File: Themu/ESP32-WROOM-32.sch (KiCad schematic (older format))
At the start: 17 parts, among them J1 USB_B_Micro, Q1 mmbt2222, Q2 mmbt2222, U1 CP2104, U3 ESP32-WROOM-32

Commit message: Routed completed
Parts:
- removed D1: RED LED, LED_SMD:LED_0603_1608Metric_Pad1.05x0.95mm_HandSolder, symbol Device:LED_Small_ALT
- added L1: RGB LED, LED APTF1616LSEEZGKQBKC:LED APTF1616LSEEZGKQBKC, symbol LED:ASMB-MTB1-0A3A2
- added R20, R21: 1K, Resistor_SMD:R_0603_1608Metric_Pad1.05x0.95mm_HandSolder, symbol Device:R_Small_US
- U3: footprint RF_Module:ESP32-WROOM-32 -> Themu_FP_Lib:ESP32WROOM32D
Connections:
- net +3V3: now also L1.4 (A); no longer R3.1
- net BTN: now also U3.10 (IO25); no longer U3.14 (IO12)
- net FLX2: now also U3.6 (IO34); no longer U3.8 (IO32)
- net FLX3: now also U3.7 (IO35); no longer U3.9 (IO33)
- net FLX4: now also U3.8 (IO32); no longer U3.6 (IO34)
- net FLX5: now also U3.9 (IO33); no longer U3.7 (IO35)
- net IO26: now reaches U3.11 (IO26)
- net IO26: now also R20.1
- net IO27: now reaches U3.12 (IO27)
- net IO27: now also R21.1
- net at R3.2: now also L1.3 (BK)
- net IO13: no longer names the net of U3.16 (IO13)
- new net: L1.1 (RK), R21.2
- new net: L1.2 (GK), R20.2
- new net IO12: R3.1, U3.14 (IO12)
- no-connect marks 33 -> 31
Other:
- moved on the sheet: R4, R5
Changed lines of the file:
@@
 	1    0    0    -1
 $EndComp
-NoConn ~ 3400 3650
-NoConn ~ 3400 3550
-NoConn ~ 3400 3450
 NoConn ~ 3400 3350
 NoConn ~ 3400 3250
@@
 ADC1_CH7
 Wire Wire Line
-	1050 3800 1500 3800
-Wire Wire Line
-	1050 3700 1050 3800
+	1100 2550 1550 2550
+Wire Wire Line
+	1100 2450 1100 2550
 $Comp
 L power:GND #PWR?
 U 1 1 5F674CFE
-P 1050 4100
+P 1100 2850
 AR Path="/5F674CFE" Ref="#PWR?"  Part="1"
 AR Path="/5F4501E0/5F674CFE" Ref="#PWR07"  Part="1"
-F 0 "#PWR07" H 1050 3850 50  0001 C CNN
-F 1 "GND" H 1055 3927 50  0000 C CNN
-F 2 "" H 1050 4100 50  0001 C CNN
-F 3 "" H 1050 4100 50  0001 C CNN
-	1    1050 4100
+F 0 "#PWR07" H 1100 2600 50  0001 C CNN
+F 1 "GND" H 1105 2677 50  0000 C CNN
+F 2 "" H 1100 2850 50  0001 C CNN
+F 3 "" H 1100 2850 50  0001 C CNN
+	1    1100 2850
 	1    0    0    -1
 $EndComp
@@
 L Device:R_Small_US R?
 U 1 1 5F674D0A
-P 1050 3600
+P 1100 2350
 AR Path="/5F674D0A" Ref="R?"  Part="1"
 AR Path="/5F4501E0/5F674D0A" Ref="R4"  Part="1"
-F 0 "R4" H 1118 3646 50  0000 L CNN
-F 1 "100K" H 1118 3555 50  0000 L CNN
-F 2 "Resistor_SMD:R_0603_1608Metric_Pad1.05x0.95mm_HandSolder" H 1050 3600 50  0001 C CNN
-F 3 "https://www.bourns.com/docs/product-datasheets/CRxxxxx.pdf" H 1050 3600 50  0001 C CNN
-F 4 "CR0603-FX-1003ELF" H 1050 3600 50  0001 C CNN "*Digikey"
-	1    1050 3600
+F 0 "R4" H 1168 2396 50  0000 L CNN
+F 1 "100K" H 1168 2305 50  0000 L CNN
+F 2 "Resistor_SMD:R_0603_1608Metric_Pad1.05x0.95mm_HandSolder" H 1100 2350 50  0001 C CNN
+F 3 "https://www.bourns.com/docs/product-datasheets/CRxxxxx.pdf" H 1100 2350 50  0001 C CNN
+F 4 "CR0603-FX-1003ELF" H 1100 2350 50  0001 C CNN "*Digikey"
+	1    1100 2350
 	1    0    0    -1
 $EndComp
@@
 L Device:R_Small_US R?
 U 1 1 5F677550
-P 1050 3950
+P 1100 2700
 AR Path="/5F677550" Ref="R?"  Part="1"
 AR Path="/5F4501E0/5F677550" Ref="R5"  Part="1"
-F 0 "R5" H 1118 3996 50  0000 L CNN
-F 1 "100K" H 1118 3905 50  0000 L CNN
-F 2 "Resistor_SMD:R_0603_1608Metric_Pad1.05x0.95mm_HandSolder" H 1050 3950 50  0001 C CNN
-F 3 "https://www.bourns.com/docs/product-datasheets/CRxxxxx.pdf" H 1050 3950 50  0001 C CNN
-F 4 "CR0603-FX-1003ELF" H 1050 3950 50  0001 C CNN "*Digikey"
-	1    1050 3950
-	1    0    0    -1
-$EndComp
-Wire Wire Line
-	1050 3800 1050 3850
-Wire Wire Line
-	1050 4050 1050 4100
-Connection ~ 1050 3800
+F 0 "R5" H 1168 2746 50  0000 L CNN
+F 1 "100K" H 1168 2655 50  0000 L CNN
+F 2 "Resistor_SMD:R_0603_1608Metric_Pad1.05x0.95mm_HandSolder" H 1100 2700 50  0001 C CNN
+F 3 "https://www.bourns.com/docs/product-datasheets/CRxxxxx.pdf" H 1100 2700 50  0001 C CNN
+F 4 "CR0603-FX-1003ELF" H 1100 2700 50  0001 C CNN "*Digikey"
+	1    1100 2700
+	1    0    0    -1
+$EndComp
+Wire Wire Line
+	1100 2550 1100 2600
+Wire Wire Line
+	1100 2800 1100 2850
+Connection ~ 1100 2550
 $Comp
 L power:+BATT #PWR06
 U 1 1 5F67B0FC
-P 1050 3500
-F 0 "#PWR06" H 1050 3350 50  0001 C CNN
-F 1 "+BATT" H 1065 3673 50  0000 C CNN
-F 2 "" H 1050 3500 50  0001 C CNN
-F 3 "" H 1050 3500 50  0001 C CNN
-	1    1050 3500
+P 1100 2250
+F 0 "#PWR06" H 1100 2100 50  0001 C CNN
+F 1 "+BATT" H 1115 2423 50  0000 C CNN
+F 2 "" H 1100 2250 50  0001 C CNN
+F 3 "" H 1100 2250 50  0001 C CNN
+	1    1100 2250
 	1    0    0    -1
 $EndComp
@@
 Wire Wire Line
 	2200 1750 2100 1750
-$Comp
-L Device:LED_Small_ALT D?
-U 1 1 5F6888D7
-P 1050 2850
-AR Path="/5F6888D7" Ref="D?"  Part="1"
-AR Path="/5F4501E0/5F6888D7" Ref="D1"  Part="1"
-F 0 "D1" V 1096 2780 50  0000 R CNN
-F 1 "RED LED" V 1005 2780 50  0000 R CNN
-F 2 "LED_SMD:LED_0603_1608Metric_Pad1.05x0.95mm_HandSolder" V 1050 2850 50  0001 C CNN
-F 3 "https://www.aopled.com/AOP_PDFs/L196L-UEC.pdf" V 1050 2850 50  0001 C CNN
-F 4 "L196L-UEC" H 1050 2850 50  0001 C CNN "*Digikey"
-	1    1050 2850
-	0    -1   -1   0
-$EndComp
 $Comp
 L power:VBUS #PWR01
@@
 Wire Wire Line
 	5100 2600 5300 2600
-Text Label 1300 3050 2    50   ~ 0
-IO13
-$Comp
-L Device:R_Small_US R3
-U 1 1 5F7258DA
-P 1050 2600
-F 0 "R3" H 1118 2646 50  0000 L CNN
-F 1 "1K" H 1118 2555 50  0000 L CNN
-F 2 "Resistor_SMD:R_0603_1608Metric_Pad1.05x0.95mm_HandSolder" H 1050 2600 50  0001 C CNN
-F 3 "https://www.bourns.com/docs/product-datasheets/CRxxxxx.pdf" H 1050 2600 50  0001 C CNN
-F 4 "CR0603-FX-1001ELF" H 1050 2600 50  0001 C CNN "*Digikey"
-	1    1050 2600
-	1    0    0    -1
-$EndComp
-Wire Wire Line
-	1050 2750 1050 2700
-Wire Wire Line
-	1050 2500 1050 2450
-Wire Wire Line
-	1050 3050 1300 3050
 NoConn ~ 6100 2400
 NoConn ~ 6100 2500
@@
 NoConn ~ 7500 1700
 NoConn ~ 7500 1600
-Text Label 3650 2450 2    50   ~ 0
-IO13
-Wire Wire Line
-	3400 2450 3650 2450
 Wire Notes Line
 	4350 850  7850 850
@@
 F 0 "U3" H 2800 4531 50  0000 C CNN
 F 1 "ESP32-WROOM-32" H 2800 4440 50  0000 C CNN
-F 2 "RF_Module:ESP32-WROOM-32" H 2800 1450 50  0001 C CNN
+F 2 "Themu_FP_Lib:ESP32WROOM32D" H 2800 1450 50  0001 C CNN
 F 3 "https://www.espressif.com/sites/default/files/documentation/esp32-wroom-32_datasheet_en.pdf" H 2500 3000 50  0001 C CNN
 F 4 "1965-ESP32-WROOM-32D(4MB)CT-ND" H 2800 2950 50  0001 C CNN "*Digikey"
@@
 Text Label 3650 2350 2    50   ~ 0
 IO12
-Text HLabel 3650 2350 2    50   Input ~ 0
+Text HLabel 3650 3450 2    50   Input ~ 0
 BTN
+Text HLabel 3850 3950 2    50   Input ~ 0
+FLX2
+Text HLabel 3850 4050 2    50   Input ~ 0
+FLX3
 Text HLabel 3850 3750 2    50   Input ~ 0
-FLX2
+FLX4
 Text HLabel 3850 3850 2    50   Input ~ 0
-FLX3
-Text HLabel 3850 3950 2    50   Input ~ 0
-FLX4
-Text HLabel 3850 4050 2    50   Input ~ 0
 FLX5
 Text HLabel 1750 2050 0    50   Input ~ 0
 FLX1
 NoConn ~ 3400 2750
-Text Label 1500 3800 2    50   ~ 0
+Text Label 1550 2550 2    50   ~ 0
 ADC1_CH0
-$Comp
-L power:+3.3V #PWR?
-U 1 1 5F795B24
-P 1050 2450
-AR Path="/5F795B24" Ref="#PWR?"  Part="1"
-AR Path="/5F4501E0/5F795B24" Ref="#PWR05"  Part="1"
-F 0 "#PWR05" H 1050 2300 50  0001 C CNN
-F 1 "+3.3V" H 1065 2623 50  0000 C CNN
-F 2 "" H 1050 2450 50  0001 C CNN
-F 3 "" H 1050 2450 50  0001 C CNN
-	1    1050 2450
-	1    0    0    -1
-$EndComp
-Wire Wire Line
-	1050 3050 1050 2950
 $Comp
 L Device:C_Small C14
@@
 	5350 1700 5150 1700
 Connection ~ 5150 1700
+$Comp
+L LED:ASMB-MTB1-0A3A2 L1
+U 1 1 5F840B4C
+P 1300 3850
+F 0 "L1" H 1300 3333 50  0000 C CNN
+F 1 "RGB LED" H 1300 3424 50  0000 C CNN
+F 2 "LED APTF1616LSEEZGKQBKC:LED APTF1616LSEEZGKQBKC" H 1300 4450 50  0001 C CNN
+F 3 "https://www.kingbrightusa.com/images/catalog/SPEC/APTF1616LSEEZGKQBKC.pdf" H 1300 3400 50  0001 C CNN
+F 4 "APTF1616LSEEZGKQBKC" H 1300 3850 50  0001 C CNN "*Digikey"
+	1    1300 3850
+	-1   0    0    1
+$EndComp
+$Comp
+L Device:R_Small_US R3
+U 1 1 5F857FC9
+P 1650 3650
+F 0 "R3" V 1550 3550 50  0000 C CNN
+F 1 "1K" V 1550 3700 50  0000 C CNN
+F 2 "Resistor_SMD:R_0603_1608Metric_Pad1.05x0.95mm_HandSolder" H 1650 3650 50  0001 C CNN
+F 3 "https://www.bourns.com/docs/product-datasheets/CRxxxxx.pdf" H 1650 3650 50  0001 C CNN
+F 4 "CR0603-FX-1001ELF" H 1650 3650 50  0001 C CNN "*Digikey"
+	1    1650 3650
+	0    1    1    0
+$EndComp
+$Comp
+L Device:R_Small_US R20
+U 1 1 5F858D55
+P 1650 3850
+F 0 "R20" V 1550 3750 50  0000 C CNN
+F 1 "1K" V 1550 3900 50  0000 C CNN
+F 2 "Resistor_SMD:R_0603_1608Metric_Pad1.05x0.95mm_HandSolder" H 1650 3850 50  0001 C CNN
+F 3 "https://www.bourns.com/docs/product-datasheets/CRxxxxx.pdf" H 1650 3850 50  0001 C CNN
+F 4 "CR0603-FX-1001ELF" H 1650 3850 50  0001 C CNN "*Digikey"
+	1    1650 3850
+	0    1    1    0
+$EndComp
+$Comp
+L Device:R_Small_US R21
+U 1 1 5F85AC5C
+P 1650 4050
+F 0 "R21" V 1550 3950 50  0000 C CNN
+F 1 "1K" V 1550 4100 50  0000 C CNN
+F 2 "Resistor_SMD:R_0603_1608Metric_Pad1.05x0.95mm_HandSolder" H 1650 4050 50  0001 C CNN
+F 3 "https://www.bourns.com/docs/product-datasheets/CRxxxxx.pdf" H 1650 4050 50  0001 C CNN
+F 4 "CR0603-FX-1001ELF" H 1650 4050 50  0001 C CNN "*Digikey"
+	1    1650 4050
+	0    1    1    0
+$EndComp
+$Comp
+L power:+3.3V #PWR?
+U 1 1 5F85EEE7
+P 1100 3350
+AR Path="/5F85EEE7" Ref="#PWR?"  Part="1"
+AR Path="/5F4501E0/5F85EEE7" Ref="#PWR03"  Part="1"
+F 0 "#PWR03" H 1100 3200 50  0001 C CNN
+F 1 "+3.3V" H 1115 3523 50  0000 C CNN
+F 2 "" H 1100 3350 50  0001 C CNN
+F 3 "" H 1100 3350 50  0001 C CNN
+	1    1100 3350
+	1    0    0    -1
+$EndComp
+Wire Wire Line
+	1100 3350 1100 3850
+Wire Wire Line
+	1500 3650 1550 3650
+Wire Wire Line
+	1500 3850 1550 3850
+Wire Wire Line
+	1550 4050 1500 4050
+Text Label 1950 3650 2    50   ~ 0
+IO12
+Text Label 1950 3850 2    50   ~ 0
+IO26
+Text Label 1950 4050 2    50   ~ 0
+IO27
+Wire Wire Line
+	1750 3650 1950 3650
+Wire Wire Line
+	1750 3850 1950 3850
+Wire Wire Line
+	1750 4050 1950 4050
+Text Label 3650 3450 2    50   ~ 0
+IO25
+Text Label 3650 3550 2    50   ~ 0
+IO26
+Text Label 3650 3650 2    50   ~ 0
+IO27
+Wire Wire Line
+	3400 3450 3650 3450
+Wire Wire Line
+	3400 3550 3650 3550
+Wire Wire Line
+	3400 3650 3650 3650
+NoConn ~ 3400 2450
 $EndSCHEMATC

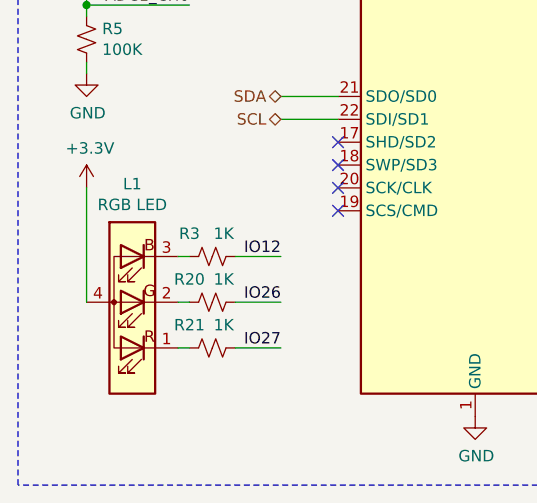
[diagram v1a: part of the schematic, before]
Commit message: RGB Led (L1) footprint updated
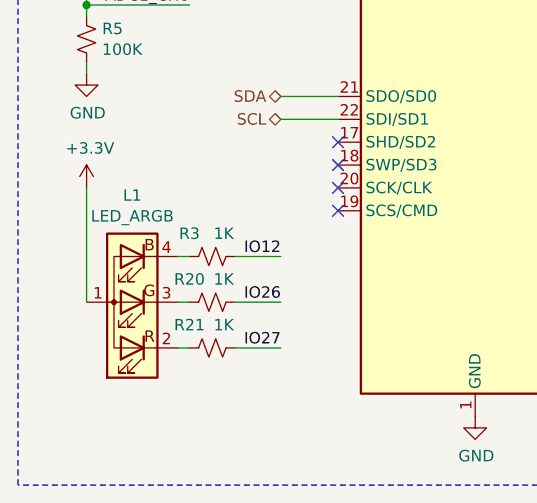
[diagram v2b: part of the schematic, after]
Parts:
- removed L1: RGB LED, LED APTF1616LSEEZGKQBKC:LED APTF1616LSEEZGKQBKC, symbol LED:ASMB-MTB1-0A3A2
- added L1: LED_ARGB, Themu_FP_Lib:LED APTF1616LSEEZGKQBKC, symbol Device:LED_ARGB
- U3: footprint Themu_FP_Lib:ESP32WROOM32D -> RF_Module:ESP32-WROOM-32
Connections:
- net +3V3: now also L1.1 (A)
- net at R21.2: now also L1.2 (RK)
- net at R20.2: now also L1.3 (GK)
- net at R3.2: now also L1.4 (BK)
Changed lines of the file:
@@
 F 0 "U3" H 2800 4531 50  0000 C CNN
 F 1 "ESP32-WROOM-32" H 2800 4440 50  0000 C CNN
-F 2 "Themu_FP_Lib:ESP32WROOM32D" H 2800 1450 50  0001 C CNN
+F 2 "RF_Module:ESP32-WROOM-32" H 2800 1450 50  0001 C CNN
 F 3 "https://www.espressif.com/sites/default/files/documentation/esp32-wroom-32_datasheet_en.pdf" H 2500 3000 50  0001 C CNN
 F 4 "1965-ESP32-WROOM-32D(4MB)CT-ND" H 2800 2950 50  0001 C CNN "*Digikey"
@@
 	5350 1700 5150 1700
 Connection ~ 5150 1700
-$Comp
-L LED:ASMB-MTB1-0A3A2 L1
-U 1 1 5F840B4C
-P 1300 3850
-F 0 "L1" H 1300 3333 50  0000 C CNN
-F 1 "RGB LED" H 1300 3424 50  0000 C CNN
-F 2 "LED APTF1616LSEEZGKQBKC:LED APTF1616LSEEZGKQBKC" H 1300 4450 50  0001 C CNN
-F 3 "https://www.kingbrightusa.com/images/catalog/SPEC/APTF1616LSEEZGKQBKC.pdf" H 1300 3400 50  0001 C CNN
-F 4 "APTF1616LSEEZGKQBKC" H 1300 3850 50  0001 C CNN "*Digikey"
-	1    1300 3850
-	-1   0    0    1
-$EndComp
 $Comp
 L Device:R_Small_US R3
@@
 	3400 3650 3650 3650
 NoConn ~ 3400 2450
+$Comp
+L Device:LED_ARGB L1
+U 1 1 5F8899CA
+P 1300 3850
+F 0 "L1" H 1300 3383 50  0000 C CNN
+F 1 "LED_ARGB" H 1300 3474 50  0000 C CNN
+F 2 "Themu_FP_Lib:LED APTF1616LSEEZGKQBKC" H 1300 3800 50  0001 C CNN
+F 3 "https://www.kingbrightusa.com/images/catalog/SPEC/APTF1616LSEEZGKQBKC.pdf" H 1300 3800 50  0001 C CNN
+F 4 "APTF1616LSEEZGKQBKC" H 1300 3850 50  0001 C CNN "*Digikey"
+	1    1300 3850
+	-1   0    0    1
+$EndComp
 $EndSCHEMATC
